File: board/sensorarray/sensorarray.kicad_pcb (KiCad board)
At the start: 2 copper layers, 31.8 x 13.5 mm, 12 parts, among them P1 CONN_5, U1 QRE1113, U2 QRE1113, U3 QRE1113

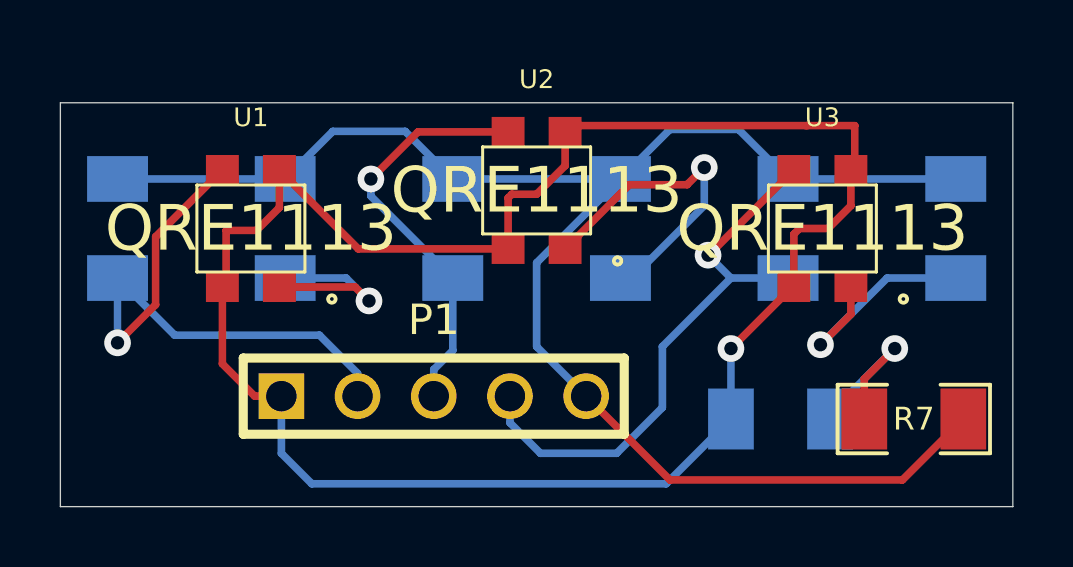
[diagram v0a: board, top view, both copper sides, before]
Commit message: Added mounting holes, removed dimensions
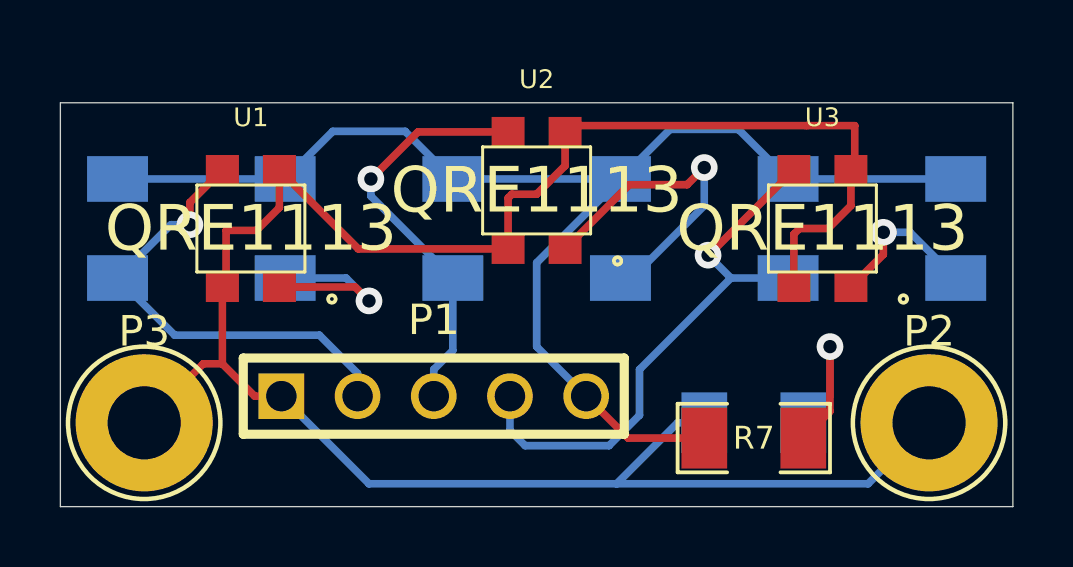
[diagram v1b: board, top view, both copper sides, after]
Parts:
- added P2: CONN_1, 2-48_mount, F.Cu at (232.4, 178.6)
- added P3: CONN_1, 2-48_mount, F.Cu at (206.2, 178.6)
- moved R7 5.37 mm to (226.6, 179.1), turned to 0 degrees
- moved D1 0.90 mm to (226.6, 178.6)
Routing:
- net 3V3: track 54.3 -> 44.2 mm
- net GND: track 64.2 -> 71.5 mm, vias 1 -> 0
- net A1: track 19.4 -> 15.5 mm
- net N-000003: track 7.77 -> 5.32 mm

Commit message: Added copper pour
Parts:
- D1: moved to F.Cu
- R7: moved to B.Cu
- moved R7 1.44 mm to (225.6, 178.1), turned to 270 degrees
- moved D1 1.14 mm to (225.6, 178.1), turned to 270 degrees
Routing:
- net GND: track 71.5 -> 0.00 mm
- net 3V3: track 44.2 -> 0.00 mm
- net A3: track 18.9 -> 22.3 mm
- net N-000008: track 10.8 -> 7.53 mm
- net A2: track 13.9 -> 15.4 mm
- net N-000003: track 5.32 -> 6.69 mm
- added copper zone on B.Cu, net 3V3
- added copper zone on F.Cu, net GND

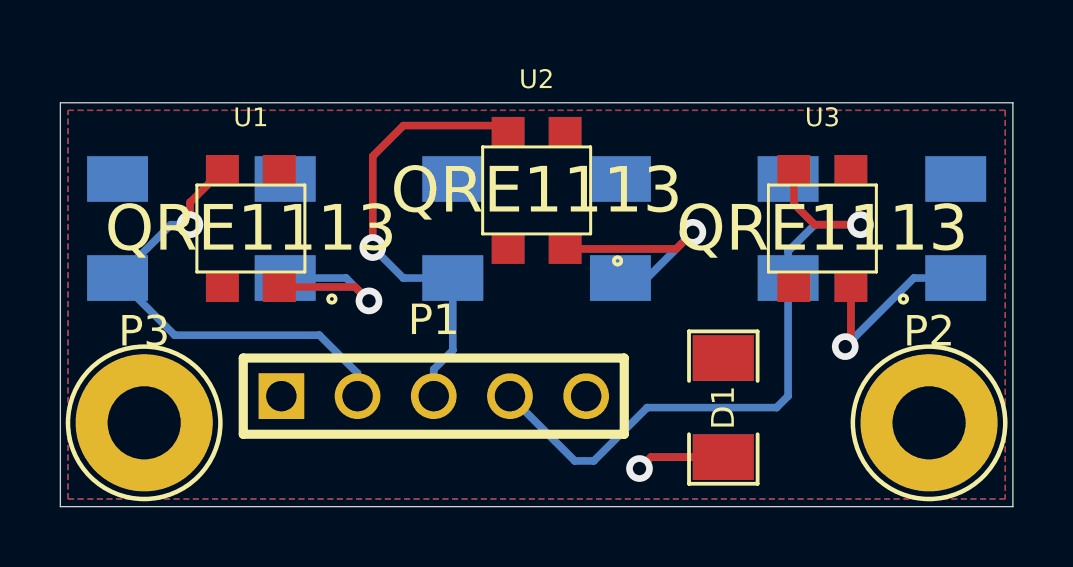
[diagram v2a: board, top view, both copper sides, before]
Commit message: Added SilkS labels for pins
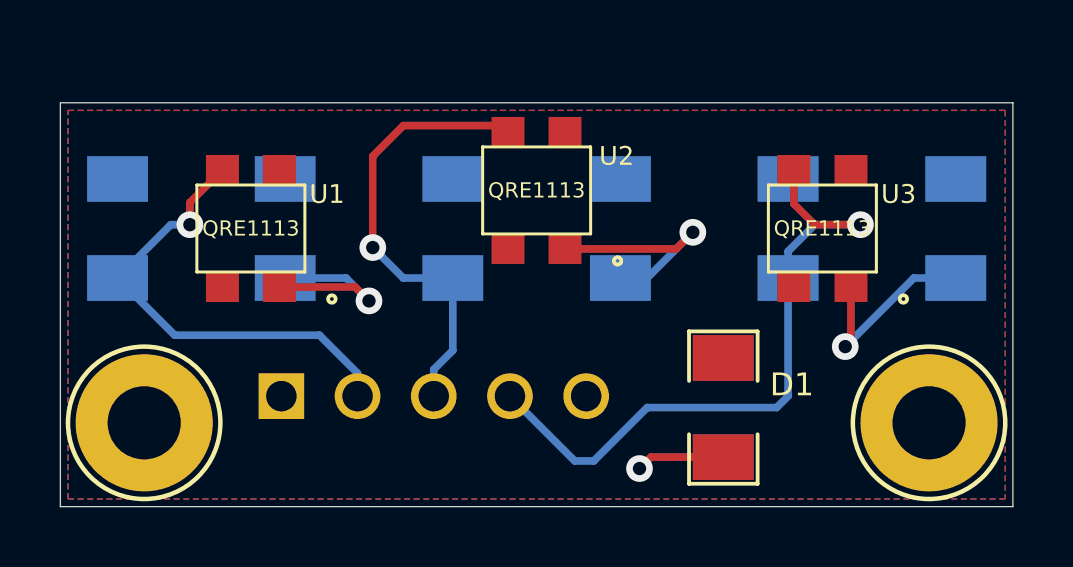
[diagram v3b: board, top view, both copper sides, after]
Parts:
- P1: moved to B.Cu
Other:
- board text added: "3V3"
- board text added: "A1"
- board text added: "A2"
- board text added: "A3"
- board text added: "GND"
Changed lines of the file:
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@@
     (links 26)
     (no_connects 0)
-    (area 202.353334 166.3715 236.304666 182.372)
+    (area 202.353334 167.740696 236.304666 182.372)
     (thickness 1.6)
-    (drawings 4)
+    (drawings 9)
     (tracks 52)
     (zones 0)
@@
   )
   (layers
-    (15 F.Cu signal)
+    (15 F.Cu signal hide)
     (0 B.Cu signal)
-    (17 F.Adhes user hide)
+    (16 B.Adhes user)
+    (17 F.Adhes user)
+    (18 B.Paste user)
     (19 F.Paste user)
-    (21 F.SilkS user)
+    (20 B.SilkS user)
+    (21 F.SilkS user hide)
+    (22 B.Mask user)
     (23 F.Mask user)
     (28 Edge.Cuts user)
@@
     (pad_to_mask_clearance 0)
     (aux_axis_origin 0 0)
-    (visible_elements 7FFFFFCF)
+    (visible_elements 7FFFFEFF)
     (pcbplotparams
       (layerselection 3178497)
@@
     (at 228.854 172.085)
     (descr "Photodetector LED combo")
-    (fp_text reference U3 (at 0 -3.7) (layer F.SilkS)
+    (fp_text reference U3 (at 2.54 -1.143) (layer F.SilkS)
       (effects (font (size 0.625 0.625) (thickness 0.1)))
     )
     (fp_text value QRE1113 (at 0 0) (layer F.SilkS)
-      (effects (font (size 1.524 1.524) (thickness 0.15)))
+      (effects (font (size 0.508 0.508) (thickness 0.0508)))
     )
     (fp_line (start -1.7 1.35) (end 1.7 1.35) (layer Dwgs.User) (width 0.1))
@@
     (at 209.804 172.085)
     (descr "Photodetector LED combo")
-    (fp_text reference U1 (at 0 -3.7) (layer F.SilkS)
+    (fp_text reference U1 (at 2.54 -1.143) (layer F.SilkS)
       (effects (font (size 0.625 0.625) (thickness 0.1)))
     )
     (fp_text value QRE1113 (at 0 0) (layer F.SilkS)
-      (effects (font (size 1.524 1.524) (thickness 0.15)))
+      (effects (font (size 0.508 0.508) (thickness 0.0508)))
     )
     (fp_line (start -1.7 1.35) (end 1.7 1.35) (layer Dwgs.User) (width 0.1))
@@
     (at 219.329 170.815)
     (descr "Photodetector LED combo")
-    (fp_text reference U2 (at 0 -3.7) (layer F.SilkS)
+    (fp_text reference U2 (at 2.667 -1.143) (layer F.SilkS)
       (effects (font (size 0.625 0.625) (thickness 0.1)))
     )
     (fp_text value QRE1113 (at 0 0) (layer F.SilkS)
-      (effects (font (size 1.524 1.524) (thickness 0.15)))
+      (effects (font (size 0.508 0.508) (thickness 0.0508)))
     )
     (fp_line (start -1.7 1.35) (end 1.7 1.35) (layer Dwgs.User) (width 0.1))
@@
     (at 210.947 172.085 270)
     (attr smd)
-    (fp_text reference R1 (at 0 0 270) (layer B.SilkS)
+    (fp_text reference R1 (at -0.635 2.159 360) (layer B.SilkS)
       (effects (font (size 0.762 0.762) (thickness 0.127)) (justify mirror))
     )
@@
     (at 205.359 172.085 270)
     (attr smd)
-    (fp_text reference R4 (at 0 0 270) (layer B.SilkS)
+    (fp_text reference R4 (at -2.667 -2.159 360) (layer B.SilkS)
       (effects (font (size 0.762 0.762) (thickness 0.127)) (justify mirror))
     )
@@
     (at 222.123 172.085 270)
     (attr smd)
-    (fp_text reference R2 (at 0 0 270) (layer B.SilkS)
+    (fp_text reference R2 (at -0.635 2.159 360) (layer B.SilkS)
       (effects (font (size 0.762 0.762) (thickness 0.127)) (justify mirror))
     )
@@
     (at 216.535 172.085 270)
     (attr smd)
-    (fp_text reference R5 (at 0 0 270) (layer B.SilkS)
+    (fp_text reference R5 (at -0.635 2.159 360) (layer B.SilkS)
       (effects (font (size 0.762 0.762) (thickness 0.127)) (justify mirror))
     )
@@
     (at 233.299 172.085 270)
     (attr smd)
-    (fp_text reference R3 (at 0 0 270) (layer B.SilkS)
+    (fp_text reference R3 (at -0.635 2.159 360) (layer B.SilkS)
       (effects (font (size 0.762 0.762) (thickness 0.127)) (justify mirror))
     )
@@
     (at 227.711 172.085 270)
     (attr smd)
-    (fp_text reference R6 (at 0 0 270) (layer B.SilkS)
+    (fp_text reference R6 (at -0.635 2.159 360) (layer B.SilkS)
       (effects (font (size 0.762 0.762) (thickness 0.127)) (justify mirror))
     )
@@
     (at 225.552 178.054 270)
     (attr smd)
-    (fp_text reference R7 (at 0 0 270) (layer B.SilkS)
+    (fp_text reference R7 (at -0.508 2.286 360) (layer B.SilkS)
       (effects (font (size 0.762 0.762) (thickness 0.127)) (justify mirror))
     )
@@
     (at 225.552 178.054 270)
     (attr smd)
-    (fp_text reference D1 (at 0 0 270) (layer F.SilkS)
+    (fp_text reference D1 (at -0.762 -2.286 360) (layer F.SilkS)
       (effects (font (size 0.762 0.762) (thickness 0.127)))
     )
@@
     )
   )
-  (module PIN_ARRAY_5x1 (layer F.Cu)
+  (module PIN_ARRAY_5x1 (layer B.Cu)
     (at 215.9 177.673)
     (descr "Double rangee de contacts 2 x 5 pins")
     (tags CONN)
-    (fp_text reference P1 (at 0 -2.54) (layer F.SilkS)
-      (effects (font (size 1.016 1.016) (thickness 0.2032)))
-    )
-    (fp_text value CONN_5 (at 0 2.54) (layer F.SilkS) hide
-      (effects (font (size 1.016 1.016) (thickness 0.2032)))
-    )
-    (fp_line (start -6.35 -1.27) (end -6.35 1.27) (layer F.SilkS) (width 0.3048))
-    (fp_line (start 6.35 1.27) (end 6.35 -1.27) (layer F.SilkS) (width 0.3048))
-    (fp_line (start -6.35 -1.27) (end 6.35 -1.27) (layer F.SilkS) (width 0.3048))
-    (fp_line (start 6.35 1.27) (end -6.35 1.27) (layer F.SilkS) (width 0.3048))
+    (fp_text reference P1 (at 0 -1.905) (layer B.SilkS)
+      (effects (font (size 1.016 1.016) (thickness 0.2032)) (justify mirror))
+    )
+    (fp_text value CONN_5 (at -4.318 -2.413) (layer B.SilkS) hide
+      (effects (font (size 1.016 1.016) (thickness 0.2032)) (justify mirror))
+    )
+    (fp_line (start -6.35 1.27) (end -6.35 -1.27) (layer B.SilkS) (width 0.3048))
+    (fp_line (start 6.35 -1.27) (end 6.35 1.27) (layer B.SilkS) (width 0.3048))
+    (fp_line (start -6.35 1.27) (end 6.35 1.27) (layer B.SilkS) (width 0.3048))
+    (fp_line (start 6.35 -1.27) (end -6.35 -1.27) (layer B.SilkS) (width 0.3048))
     (pad 1 thru_hole rect (at -5.08 0) (size 1.524 1.524) (drill 1.016)
-      (layers *.Cu *.Mask F.SilkS)
+      (layers *.Cu *.Mask B.SilkS)
       (net 5 GND)
     )
     (pad 2 thru_hole circle (at -2.54 0) (size 1.524 1.524) (drill 1.016)
-      (layers *.Cu *.Mask F.SilkS)
+      (layers *.Cu *.Mask B.SilkS)
       (net 2 A1)
     )
     (pad 3 thru_hole circle (at 0 0) (size 1.524 1.524) (drill 1.016)
-      (layers *.Cu *.Mask F.SilkS)
+      (layers *.Cu *.Mask B.SilkS)
       (net 3 A2)
     )
     (pad 4 thru_hole circle (at 2.54 0) (size 1.524 1.524) (drill 1.016)
-      (layers *.Cu *.Mask F.SilkS)
+      (layers *.Cu *.Mask B.SilkS)
       (net 4 A3)
     )
     (pad 5 thru_hole circle (at 5.08 0) (size 1.524 1.524) (drill 1.016)
-      (layers *.Cu *.Mask F.SilkS)
+      (layers *.Cu *.Mask B.SilkS)
       (net 1 3V3)
     )
@@
     (descr "module 1 pin (ou trou mecanique de percage)")
     (tags DEV)
-    (fp_text reference P2 (at 0 -3.048) (layer F.SilkS)
+    (fp_text reference P2 (at 0 -3.048) (layer F.SilkS) hide
       (effects (font (size 1.016 1.016) (thickness 0.254)))
     )
@@
     (descr "module 1 pin (ou trou mecanique de percage)")
     (tags DEV)
-    (fp_text reference P3 (at 0 -3.048) (layer F.SilkS)
+    (fp_text reference P3 (at 0 -3.048) (layer F.SilkS) hide
       (effects (font (size 1.016 1.016) (thickness 0.254)))
     )
@@
     )
   )
+  (gr_text 3V3 (at 220.98 179.578) (layer B.SilkS)
+    (effects (font (size 0.508 0.508) (thickness 0.0508)) (justify mirror))
+  )
+  (gr_text A3 (at 218.44 179.578) (layer B.SilkS)
+    (effects (font (size 0.508 0.508) (thickness 0.0508)) (justify mirror))
+  )
+  (gr_text A2 (at 215.9 179.578) (layer B.SilkS)
+    (effects (font (size 0.508 0.508) (thickness 0.0508)) (justify mirror))
+  )
+  (gr_text A1 (at 213.36 179.578) (layer B.SilkS)
+    (effects (font (size 0.508 0.508) (thickness 0.0508)) (justify mirror))
+  )
+  (gr_text GND (at 210.82 179.578) (layer B.SilkS)
+    (effects (font (size 0.508 0.508) (thickness 0.0508)) (justify mirror))
+  )
   (gr_line (start 203.454 181.356) (end 203.454 167.894) (angle 90) (layer Edge.Cuts) (width 0.0254))
